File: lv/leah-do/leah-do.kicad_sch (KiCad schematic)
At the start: 4 parts, among them J1 AudioJack4, U1 MAX98357A

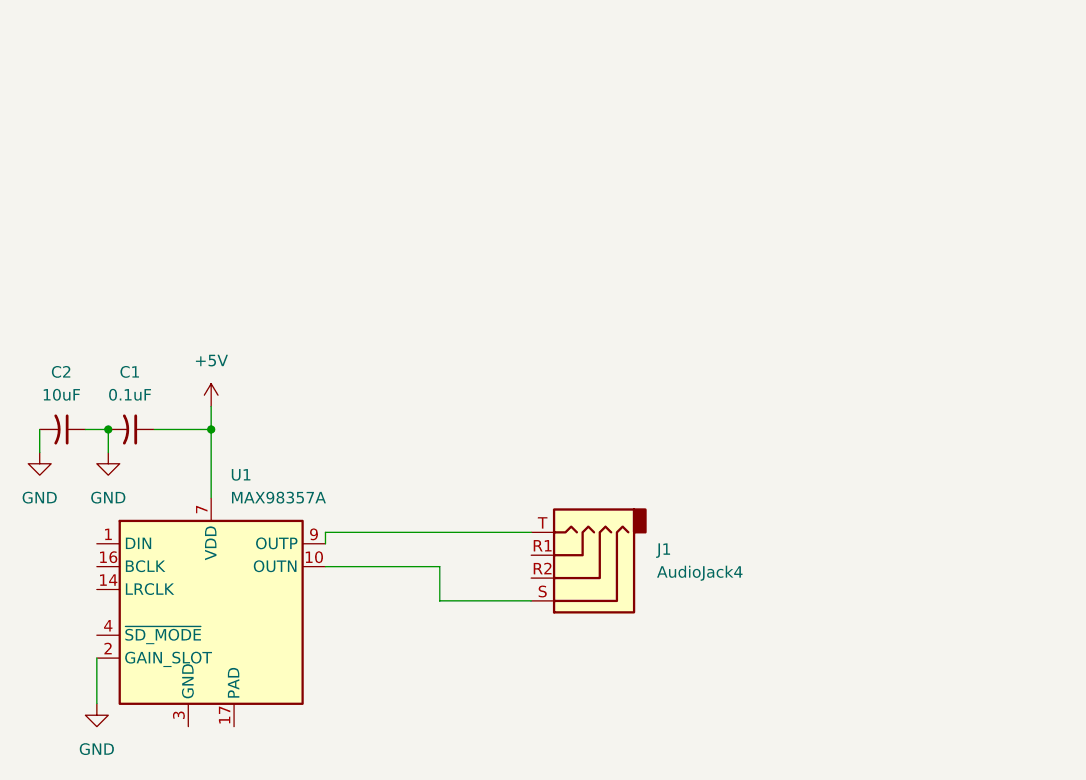
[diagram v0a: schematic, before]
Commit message: Updated breakout schematic, uploaded symbol for IC
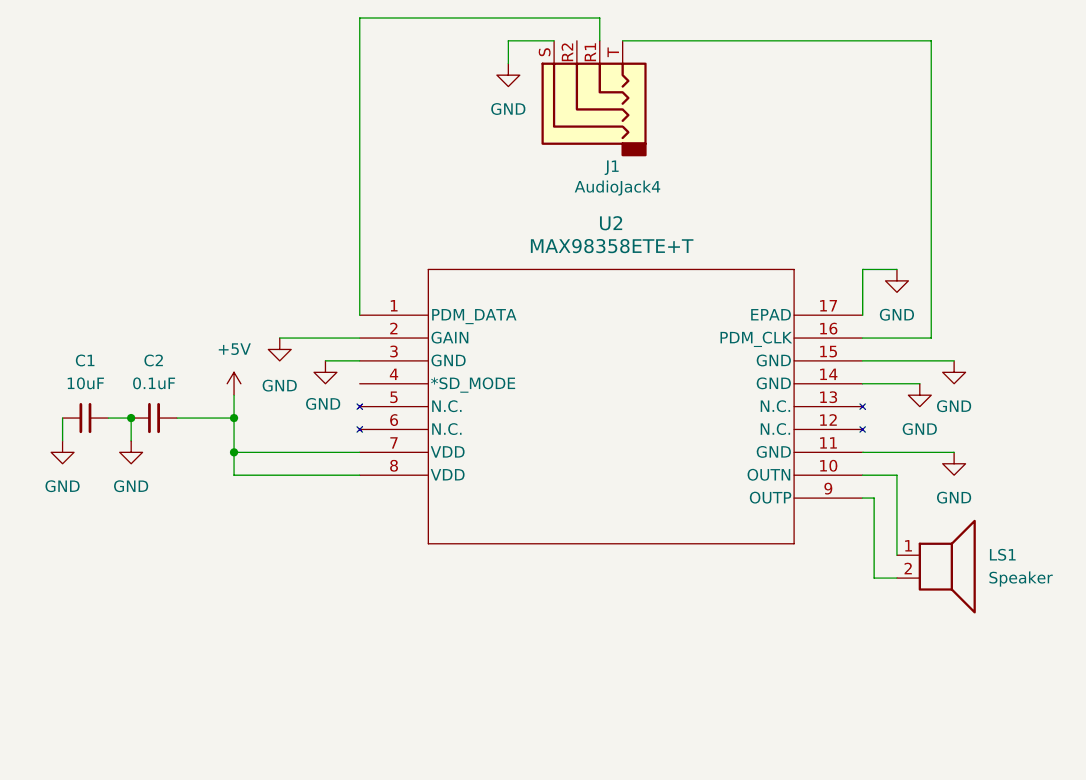
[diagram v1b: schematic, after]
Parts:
- removed C1: 0.1uF, symbol Device:C_Small_US
- removed C2: 10uF, symbol Device:C_Small_US
- removed U1: MAX98357A, Package_DFN_QFN:TQFN-16-1EP_3x3mm_P0.5mm_EP1.23x1.23mm, symbol Audio:MAX98357A
- added C1: 10uF, symbol Device:C_Small
- added C2: 0.1uF, symbol Device:C_Small
- added LS1: Speaker, symbol Device:Speaker
- added U2: MAX98358ETE+T, 21-0136_T1633+4_MXM, symbol MAX98358 IC:MAX98358ETE+T
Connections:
- net +5V: now also C2.1, U2.7 (VDD), U2.8 (VDD)
- net GND: now also J1.S, C1.1, C1.2, C2.2, U2.11 (GND), U2.14 (GND), U2.15 (GND), U2.17 (EPAD), U2.2 (GAIN), U2.3 (GND)
- net at J1.R1: now also U2.1 (PDM_DATA)
- net at J1.T: now also U2.16 (PDM_CLK)
- new net: LS1.1, U2.10 (OUTN)
- new net: LS1.2, U2.9 (OUTP)
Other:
- moved on the sheet: J1
